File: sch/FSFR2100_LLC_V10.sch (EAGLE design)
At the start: 130 parts, among them IC1 FSFR2100, J1 J5MM, J2 J5MM, P1 10k, P2 10k, P3 10K, Q1 BC856ASMD, Q2 BC846ASMD

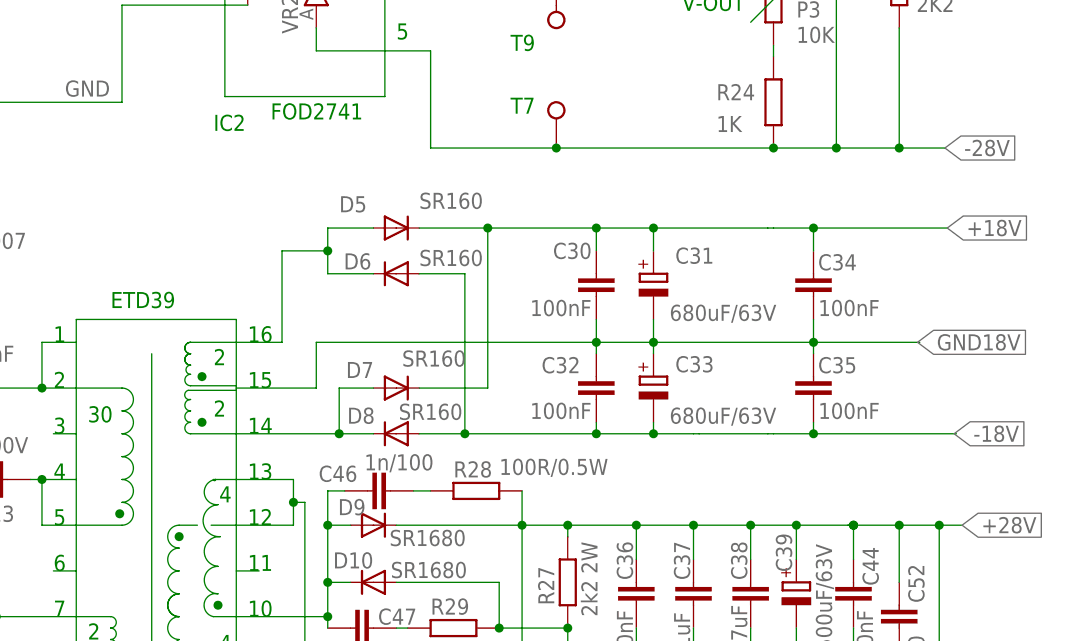
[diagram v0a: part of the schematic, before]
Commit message: Transformer Secondary Slave 2x18v 14pin_Gnd
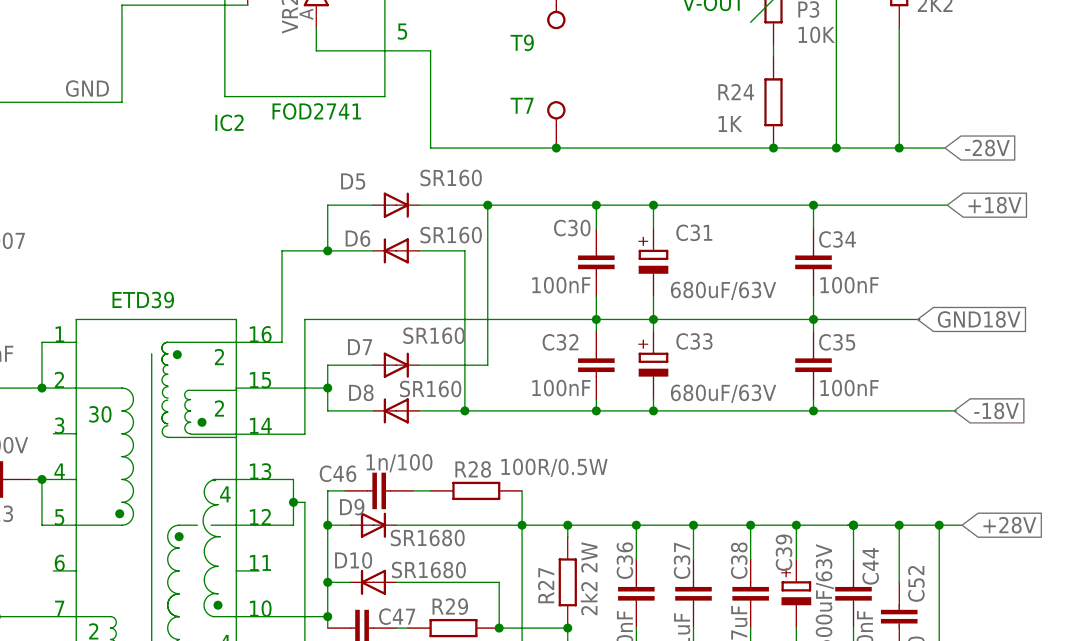
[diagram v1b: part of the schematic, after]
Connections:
- removed net N$67: D7.A, D8.C
- net GND: now also D7.A, D8.C
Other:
- moved on the sheet: C30, C31, C32, C33, C34, C35, D5, D6, D7, D8
